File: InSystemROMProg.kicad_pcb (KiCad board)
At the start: 2 copper layers, 48.2 x 65.1 mm, 6 parts, among them J1 Conn_02x14_Counter_Clockwise, J2 Conn_02x20_Counter_Clockwise, J3 Conn_01x05, U1 SST39SF040-70-4C-PHE

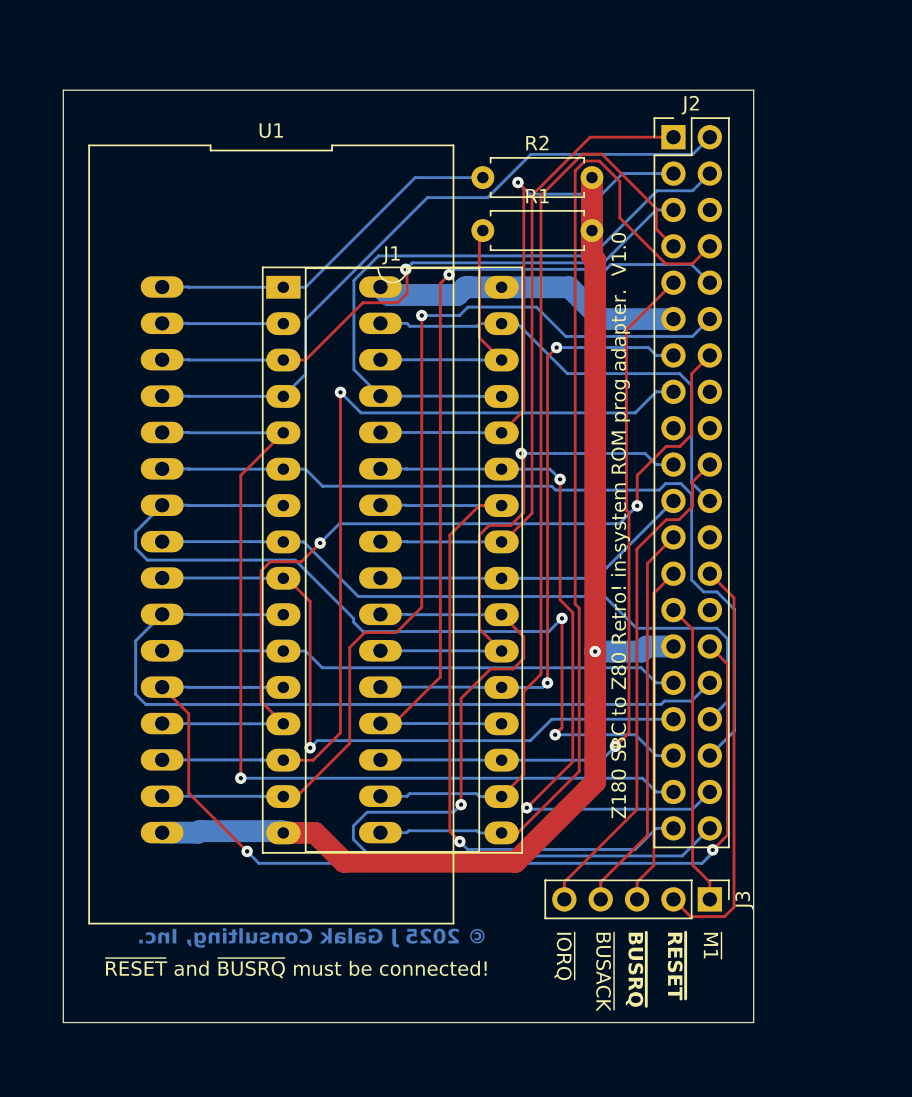
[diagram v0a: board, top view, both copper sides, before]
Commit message: Version 1.1 - pinout and pullups fixed, but untested
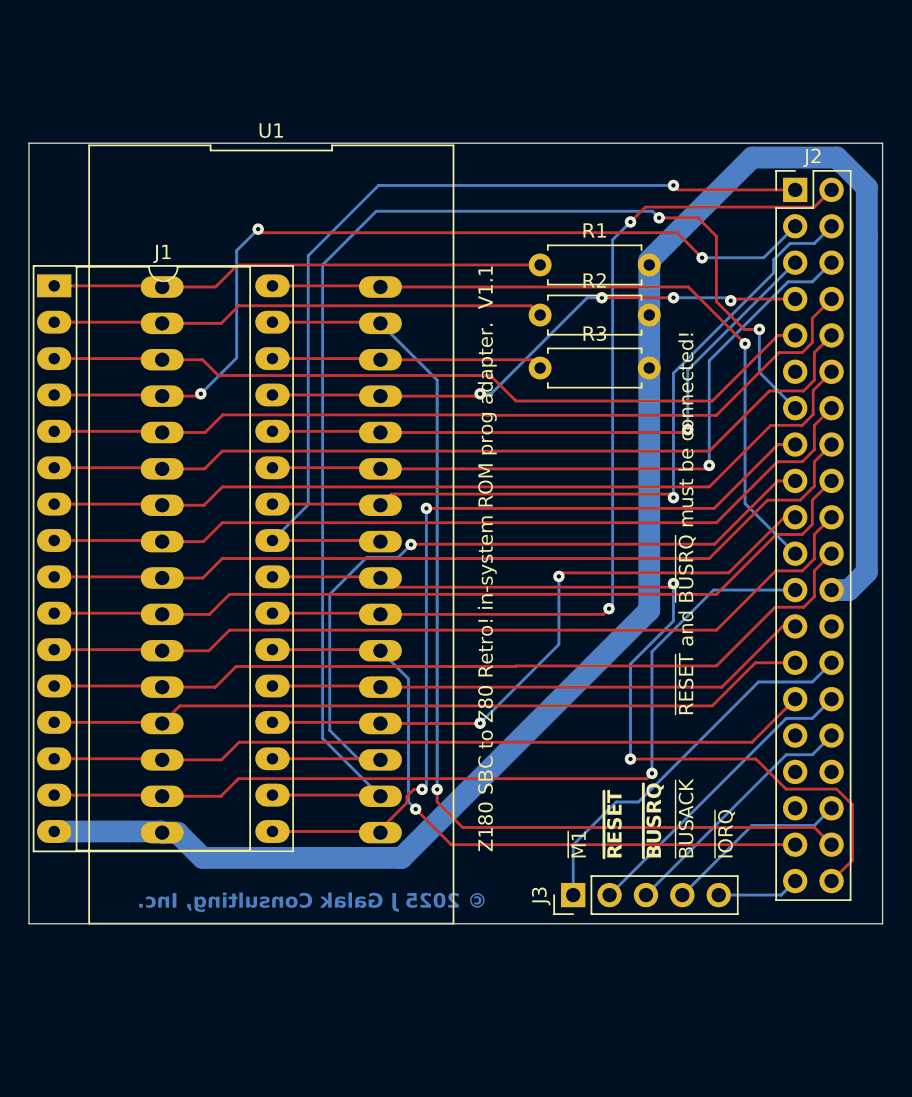
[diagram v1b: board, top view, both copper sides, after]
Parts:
- added R2: 10K, Resistor_THT:R_Axial_DIN0207_L6.3mm_D2.5mm_P7.62mm_Horizontal, F.Cu at (110.7, -3.00)
- J2: footprint Connector_PinHeader_2.54mm:PinHeader_2x20_P2.54mm_Vertical -> JgalakLib:PinHeader_2x20_P2.54mm_Vertical
- moved J1 16.0 mm to (76.8, -5.04)
- moved R3 10.4 mm to (110.7, 0.70)
- moved J3 9.54 mm to (113.0, 37.5), turned to 90 degrees
- moved J2 9.26 mm to (128.5, -11.7)
- moved R1 7.29 mm to (110.7, -6.50)
- renumbered R2 to R1, R1 to R3
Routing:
- net /~{RD}: track 22.7 -> 64.5 mm, vias 0 -> 2
- net GND: track 81.4 -> 122.8 mm, vias 1 -> 0
- net /~{WR}: track 32.3 -> 71.3 mm, vias 0 -> 1
- net /~{IORQ}: track 35.1 -> 5.75 mm
- net +5V: track 21.8 -> 50.7 mm, vias 0 -> 1
- net /A16: track 8.47 -> 34.7 mm
- net /D4: track 65.7 -> 90.9 mm, vias 0 -> 2
- net /A1: track 36.6 -> 59.2 mm
- net /A11: track 45.2 -> 64.7 mm, vias 0 -> 1
- net /D6: track 61.4 -> 45.2 mm, vias 1 -> 2
- net /A12: track 48.0 -> 63.0 mm, vias 0 -> 3
- net /~{BUSACK}: track 27.4 -> 12.9 mm
- net /A15: track 41.4 -> 55.5 mm, vias 1 -> 0
- net /D3: track 72.5 -> 59.4 mm, vias 0 -> 2
- net /A3: track 47.4 -> 59.2 mm, vias 1 -> 0
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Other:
- board size 48.2 x 65.1 mm -> 59.6 x 54.5 mm
- board text added: "Z180 SBC to Z80 Retro! in-system ROM prog adapter. V1.1"
- board text removed: "Z180 SBC to Z80 Retro! in-system ROM prog adapter. V1.0"
